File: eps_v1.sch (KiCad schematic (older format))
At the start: 11 parts

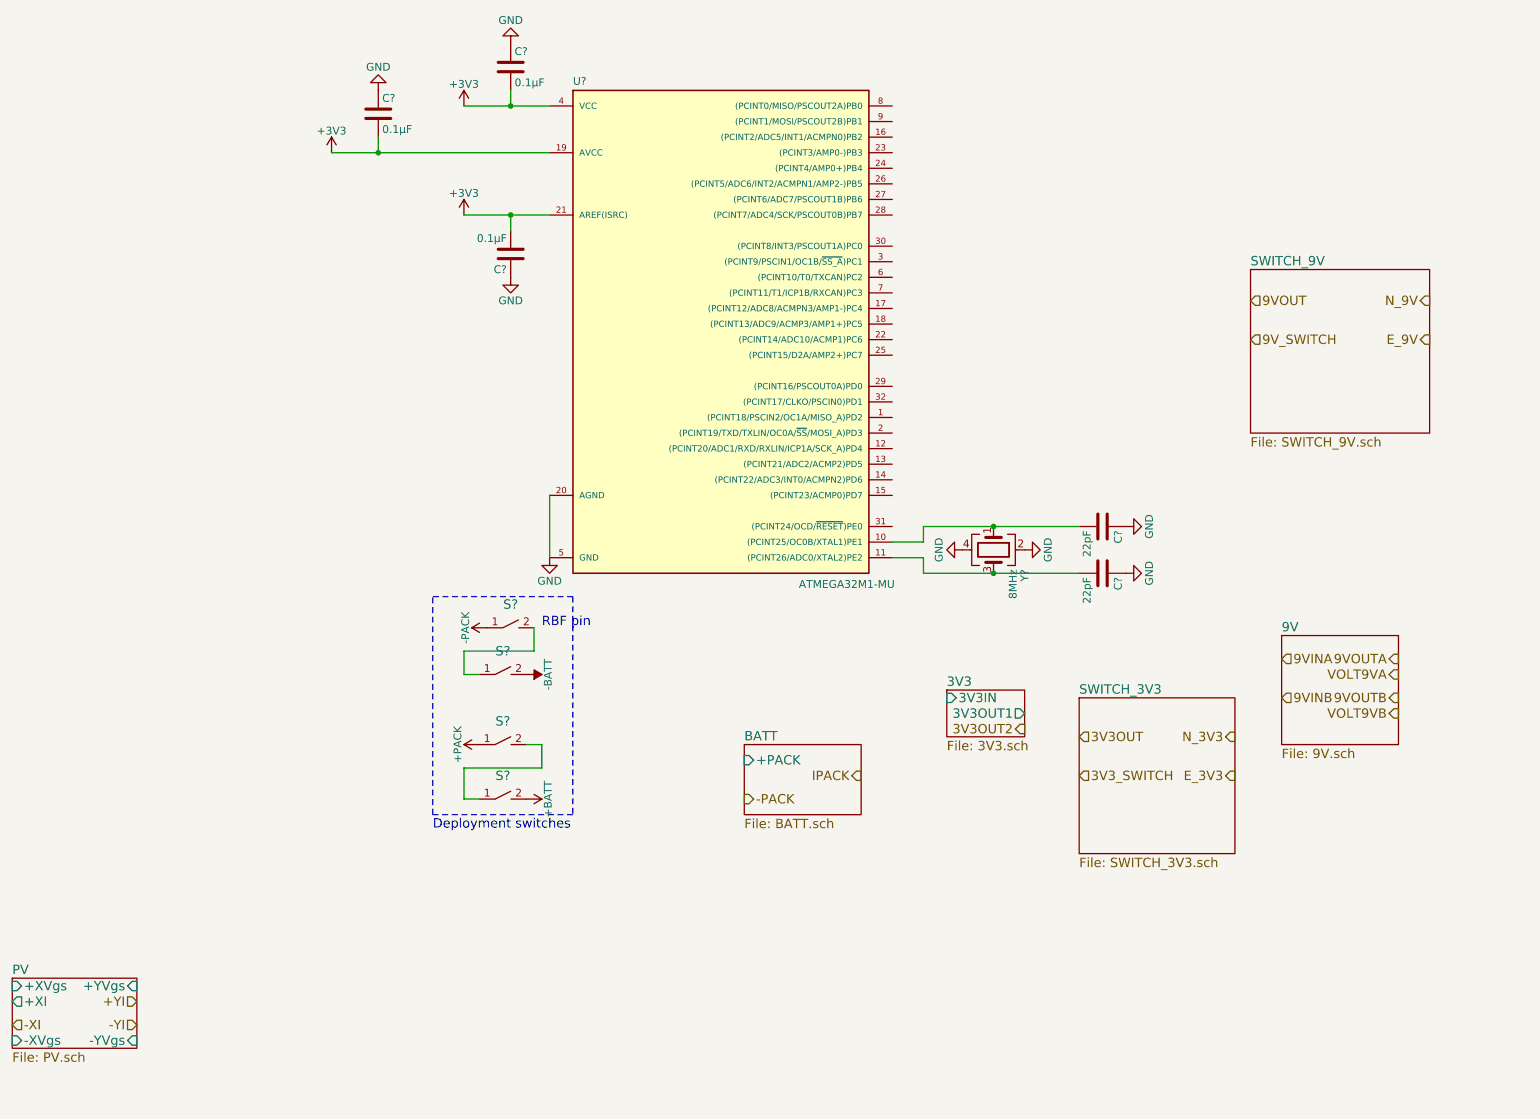
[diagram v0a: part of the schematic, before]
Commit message: Began interfacing with µC
Also all 9V should now be 5V, change resistors accordingly.
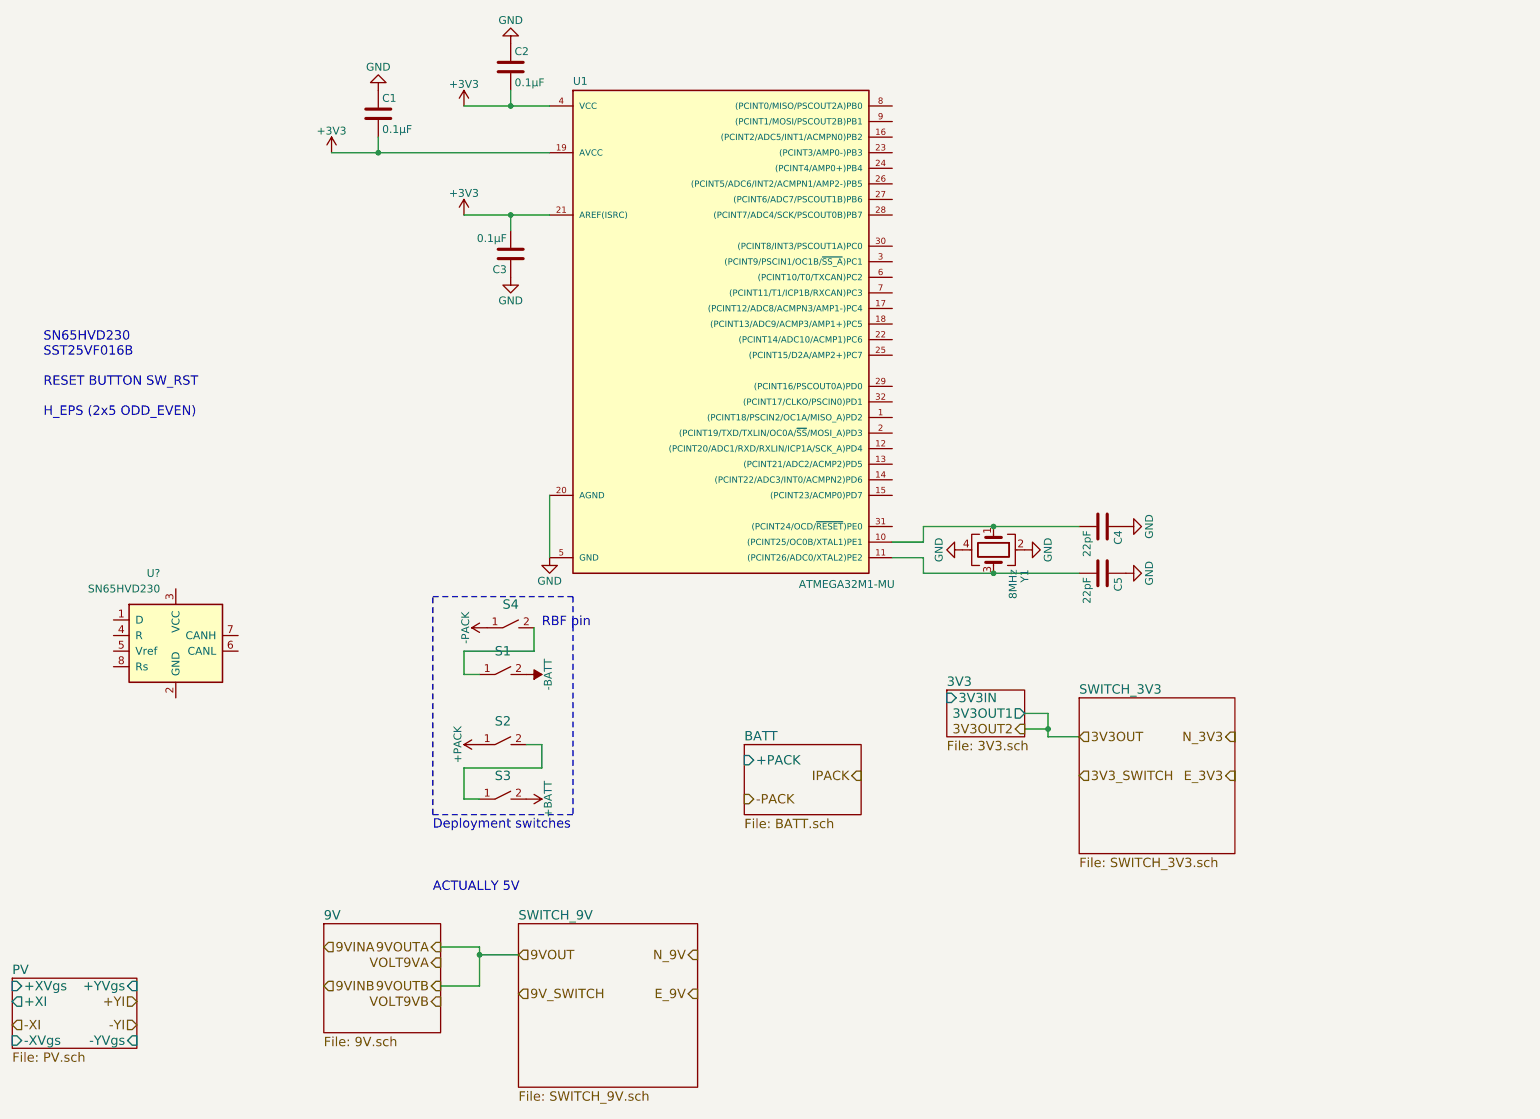
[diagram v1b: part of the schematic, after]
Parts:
- added U?: SN65HVD230, Housings_SOIC:SOIC-8_3.9x4.9mm_Pitch1.27mm, symbol SN65HVD230
- C1, C2, C3, C4, C5: renamed from C?; footprint (none) -> Capacitors_SMD:C_0603_HandSoldering
- Y1: renamed from Y?; footprint (none) -> Housings_SOIC:SO-20_12.8x7.5mm_Pitch1.27mm
- gave numbers to parts that had none: 5
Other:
- note added: "ACTUALLY 5V"
- note added: "SN65HVD230\nSST25VF016B\n\nRESET BUTTON SW_RST\n\nH_EPS (2x5 ODD_EVEN)"
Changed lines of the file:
@@
 LIBS:ina214
 LIBS:tps61088
+LIBS:cdh_lib
 LIBS:eps_v1-cache
 EELAYER 25 0
@@
 $EndDescr
 $Comp
-L switch S?
+L switch S1
 U 1 1 5998D4E2
 P 4700 4950
-F 0 "S?" H 4700 5100 60  0000 C CNN
+F 0 "S1" H 4700 5100 60  0000 C CNN
 F 1 "switch" H 4700 4900 60  0001 C CNN
 F 2 "" H 4700 4950 60  0001 C CNN
@@
 $EndComp
 $Comp
-L switch S?
+L switch S2
 U 1 1 59990767
 P 4700 5400
-F 0 "S?" H 4700 5550 60  0000 C CNN
+F 0 "S2" H 4700 5550 60  0000 C CNN
 F 1 "switch" H 4700 5350 60  0001 C CNN
 F 2 "" H 4700 5400 60  0001 C CNN
@@
 $EndComp
 $Comp
-L switch S?
+L switch S3
 U 1 1 59990813
 P 4700 5750
-F 0 "S?" H 4700 5900 60  0000 C CNN
+F 0 "S3" H 4700 5900 60  0000 C CNN
 F 1 "switch" H 4700 5700 60  0001 C CNN
 F 2 "" H 4700 5750 60  0001 C CNN
@@
 $EndComp
 $Comp
-L switch S?
+L switch S4
 U 1 1 59990A70
 P 4750 4650
-F 0 "S?" H 4750 4800 60  0000 C CNN
+F 0 "S4" H 4750 4800 60  0000 C CNN
 F 1 "switch" H 4750 4600 60  0001 C CNN
 F 2 "" H 4750 4650 60  0001 C CNN
@@
 -YI
 $Sheet
-S 9700 4700 750  700
+S 3550 6550 750  700
 U 5A1A5B75
 F0 "9V" 60
@@
 3V3_SWITCH
 $Sheet
-S 9500 2350 1150 1050
+S 4800 6550 1150 1050
 U 5A234549
 F0 "SWITCH_9V" 60
 F1 "SWITCH_9V.sch" 60
 $EndSheet
-Text HLabel 9500 2550 2    60   Input ~ 0
+Text HLabel 4800 6750 2    60   Input ~ 0
 9VOUT
-Text HLabel 9500 2800 2    60   Input ~ 0
+Text HLabel 4800 7000 2    60   Input ~ 0
 9V_SWITCH
-Text HLabel 10650 2550 0    60   Output ~ 0
+Text HLabel 5950 6750 0    60   Output ~ 0
 N_9V
-Text HLabel 10650 2800 0    60   Output ~ 0
+Text HLabel 5950 7000 0    60   Output ~ 0
 E_9V
 Text HLabel 9400 5600 0    60   Output ~ 0
 E_3V3
-Text HLabel 9700 4850 2    60   Input ~ 0
+Text HLabel 3550 6700 2    60   Input ~ 0
 9VINA
-Text HLabel 9700 5100 2    60   Input ~ 0
+Text HLabel 3550 6950 2    60   Input ~ 0
 9VINB
-Text HLabel 10450 4850 0    60   Output ~ 0
+Text HLabel 4300 6700 0    60   Output ~ 0
 9VOUTA
-Text HLabel 10450 4950 0    60   Output ~ 0
+Text HLabel 4300 6800 0    60   Output ~ 0
 VOLT9VA
-Text HLabel 10450 5100 0    60   Output ~ 0
+Text HLabel 4300 6950 0    60   Output ~ 0
 9VOUTB
-Text HLabel 10450 5200 0    60   Output ~ 0
+Text HLabel 4300 7050 0    60   Output ~ 0
 VOLT9VB
 Text HLabel 8050 5300 0    60   Output ~ 0
@@
 Connection ~ 4750 1300
 $Comp
-L C C?
+L C C2
 U 1 1 5A75F62F
 P 4750 1050
-F 0 "C?" H 4775 1150 50  0000 L CNN
+F 0 "C2" H 4775 1150 50  0000 L CNN
 F 1 "0.1µF" H 4775 950 50  0000 L CNN
-F 2 "" H 4788 900 50  0001 C CNN
+F 2 "Capacitors_SMD:C_0603_HandSoldering" H 4788 900 50  0001 C CNN
 F 3 "" H 4750 1050 50  0001 C CNN
 	1    4750 1050
@@
 Connection ~ 3900 1600
 $Comp
-L C C?
+L C C1
 U 1 1 5A75F878
 P 3900 1350
-F 0 "C?" H 3925 1450 50  0000 L CNN
+F 0 "C1" H 3925 1450 50  0000 L CNN
 F 1 "0.1µF" H 3925 1250 50  0000 L CNN
-F 2 "" H 3938 1200 50  0001 C CNN
+F 2 "Capacitors_SMD:C_0603_HandSoldering" H 3938 1200 50  0001 C CNN
 F 3 "" H 3900 1350 50  0001 C CNN
 	1    3900 1350
@@
 Connection ~ 4750 2000
 $Comp
-L C C?
+L C C3
 U 1 1 5A75F9D3
 P 4750 2250
-F 0 "C?" H 4775 2350 50  0000 L CNN
+F 0 "C3" H 4775 2350 50  0000 L CNN
 F 1 "0.1µF" H 4775 2150 50  0000 L CNN
-F 2 "" H 4788 2100 50  0001 C CNN
+F 2 "Capacitors_SMD:C_0603_HandSoldering" H 4788 2100 50  0001 C CNN
 F 3 "" H 4750 2250 50  0001 C CNN
 	1    4750 2250
@@
 $EndComp
 $Comp
-L Crystal_GND24 Y?
+L Crystal_GND24 Y1
 U 1 1 5A760437
 P 7850 4150
-F 0 "Y?" H 7975 4350 50  0000 L CNN
+F 0 "Y1" H 7975 4350 50  0000 L CNN
 F 1 "8MHz" H 7975 4275 50  0000 L CNN
-F 2 "" H 7850 4150 50  0001 C CNN
+F 2 "Housings_SOIC:SO-20_12.8x7.5mm_Pitch1.27mm" H 7850 4150 50  0001 C CNN
 F 3 "" H 7850 4150 50  0001 C CNN
 	1    7850 4150
@@
 	7400 4200 7200 4200
 $Comp
-L C C?
+L C C4
 U 1 1 5A760A5E
 P 8550 4000
-F 0 "C?" H 8575 4100 50  0000 L CNN
+F 0 "C4" H 8575 4100 50  0000 L CNN
 F 1 "22pF" H 8575 3900 50  0000 L CNN
-F 2 "" H 8588 3850 50  0001 C CNN
+F 2 "Capacitors_SMD:C_0603_HandSoldering" H 8588 3850 50  0001 C CNN
 F 3 "" H 8550 4000 50  0001 C CNN
 	1    8550 4000
@@
 Connection ~ 7850 4000
 $Comp
-L C C?
+L C C5
 U 1 1 5A760D00
 P 8550 4300
-F 0 "C?" H 8575 4400 50  0000 L CNN
+F 0 "C5" H 8575 4400 50  0000 L CNN
 F 1 "22pF" H 8575 4200 50  0000 L CNN
-F 2 "" H 8588 4150 50  0001 C CNN
+F 2 "Capacitors_SMD:C_0603_HandSoldering" H 8588 4150 50  0001 C CNN
 F 3 "" H 8550 4300 50  0001 C CNN
 	1    8550 4300
@@
 $EndComp
 $Comp
-L ATMEGA32M1-MU U?
+L ATMEGA32M1-MU U1
 U 1 1 5A761CDE
 P 6100 3000
-F 0 "U?" H 5150 4830 50  0000 L BNN
+F 0 "U1" H 5150 4830 50  0000 L BNN
 F 1 "ATMEGA32M1-MU" H 6600 1600 50  0000 L BNN
 F 2 "QFN32" H 6100 3000 50  0001 C CIN
@@
 	1    0    0    -1
 $EndComp
+Text Notes 1750 3300 0    60   ~ 0
+SN65HVD230\nSST25VF016B\n\nRESET BUTTON SW_RST\n\nH_EPS (2x5 ODD_EVEN)
+Wire Wire Line
+	8050 5300 8200 5300
+Wire Wire Line
+	8200 5200 8200 5350
+Wire Wire Line
+	8200 5350 8400 5350
+Wire Wire Line
+	8050 5200 8200 5200
+Connection ~ 8200 5300
+Wire Wire Line
+	4300 6700 4550 6700
+Wire Wire Line
+	4550 6700 4550 6950
+Wire Wire Line
+	4550 6750 4800 6750
+Wire Wire Line
+	4550 6950 4300 6950
+Connection ~ 4550 6750
+Text Notes 4250 6350 0    60   ~ 0
+ACTUALLY 5V
+$Comp
+L SN65HVD230 U?
+U 1 1 5A764293
+P 2600 4700
+F 0 "U?" H 2500 5100 50  0000 R CNN
+F 1 "SN65HVD230" H 2500 5000 50  0000 R CNN
+F 2 "Housings_SOIC:SOIC-8_3.9x4.9mm_Pitch1.27mm" H 2600 4200 50  0001 C CNN
+F 3 "" H 2500 5100 50  0001 C CNN
+	1    2600 4700
+	1    0    0    -1
+$EndComp

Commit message: PCB layout as of 2018-02-07
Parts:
- added C6: 0.1µF, Capacitors_SMD:C_0603_HandSoldering, symbol C
- added C7: 100nF, Capacitors_SMD:C_0603_HandSoldering, symbol C
- added J7: PROGRAMMING PORT, Pin_Headers:Pin_Header_Straight_2x03_Pitch2.54mm, symbol Conn_02x03_Odd_Even
- added J8: H_EPS, Pin_Headers:Pin_Header_Straight_2x05_Pitch2.54mm, symbol Conn_02x05_Odd_Even
- added R5: 1kΩ, Resistors_SMD:R_0603_HandSoldering, symbol R
- added R6: 120Ω, Resistors_SMD:R_0603_HandSoldering, symbol R
- added R7: 10kΩ, Resistors_SMD:R_0603_HandSoldering, symbol R
- added SW1: SW_RST, symbol SW_Push_Dual
- added U9: SST25VF016B, kicad-libraries:SOIC8, symbol SST25VF016B
- U1: footprint QFN32 -> Housings_DFN_QFN:QFN-32-1EP_7x7mm_Pitch0.65mm
- U8: renamed from U?; footprint Housings_SOIC:SOIC-8_3.9x4.9mm_Pitch1.27mm -> (none)
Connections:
- net +3V3: now also U8.3 (VCC), C6.2, C7.1, J7.2 (Pin_2), J8.2 (Pin_2), R7.1, U9.3 (WPn), U9.7 (HOLDn), U9.8 (Vdd)
- net GND: now also U8.2 (GND), C6.1, C7.2, J7.6 (Pin_6), J8.10 (Pin_10), J8.9 (Pin_9), R5.2, SW1.2, SW1.4, U9.4 (Vss)
- net MISO_A: now reaches U1.1 ((PCINT18/PSCIN2/OC1A/MISO_A)PD2)
- net MISO_A: now also J7.1 (Pin_1)
- net SCK_A: now reaches U1.12 ((PCINT20/ADC1/RXD/RXLIN/ICP1A/SCK_A)PD4)
- net SCK_A: now also J7.3 (Pin_3)
- net CAN_LPWR: now reaches U1.16 ((PCINT2/ADC5/INT1/ACMPN0)PB2)
- net CAN_LPWR: now also U8.8 (Rs), R5.1
- net MOSI_A: now reaches U1.2 ((PCINT19/TXD/TXLIN/OC0A/~SS~/MOSI_A)PD3)
- net MOSI_A: now also J7.4 (Pin_4)
- net CS_MEM: now reaches U1.26 ((PCINT5/ADC6/INT2/ACMPN1/AMP2-)PB5)
- net CS_MEM: now also U9.1 (CEn)
- net SCK: now reaches U1.28 ((PCINT7/ADC4/SCK/PSCOUT0B)PB7)
- net SCK: now also U9.6 (SCK)
- net at U1.31 ((PCINT24/OCD/~RESET~)PE0): now also R7.2, SW1.1, SW1.3
- net CAN_TX: now reaches U1.6 ((PCINT10/T0/TXCAN)PC2)
- net CAN_TX: now also U8.1 (D)
- net CAN_RX: now reaches U1.7 ((PCINT11/T1/ICP1B/RXCAN)PC3)
- net CAN_RX: now also U8.4 (R)
- net MISO: now reaches U1.8 ((PCINT0/MISO/PSCOUT2A)PB0)
- net MISO: now also U9.2 (SO)
- net MOSI: now reaches U1.9 ((PCINT1/MOSI/PSCOUT2B)PB1)
- net MOSI: now also U9.5 (SI)
- net CANL: now reaches U8.6 (CANL)
- net CANL: now also J8.8 (Pin_8), R6.2
- net CANH: now reaches U8.7 (CANH)
- net CANH: now also J8.6 (Pin_6), R6.1
- new net +5V: J8.1 (Pin_1)
- new net EPS_RST: J8.7 (Pin_7)
- new net RST: J7.5 (Pin_5)
- no-connect marks 0 -> 4
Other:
- note removed: "SN65HVD230\nSST25VF016B\n\nRESET BUTTON SW_RST\n\nH_EPS (2x5 ODD_EVEN)"
